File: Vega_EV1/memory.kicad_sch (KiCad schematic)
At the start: 15 parts, among them J10 1.5MB RAM Expansion, J14 Flash WR EN, J27 EXTRAM_ENABLE, P1 60 Pin Edge Conn, U5 74AHCT273, U6 74AHCT273, U7 SST39SF040, U8 AS6C1008-55PCN, U9 AS6C4008-55PCN

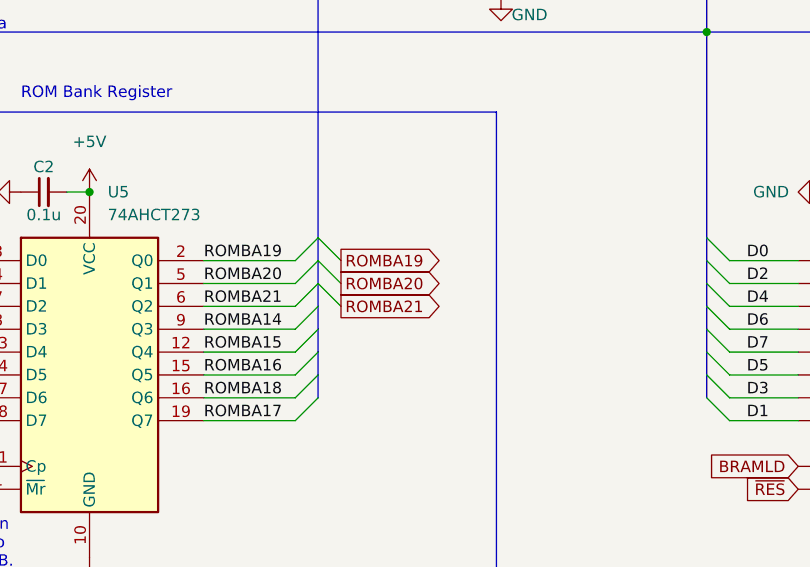
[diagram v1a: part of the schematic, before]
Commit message: More space between Edge and YM2151 Add IEC logic back in IDC headers for NES and IEC
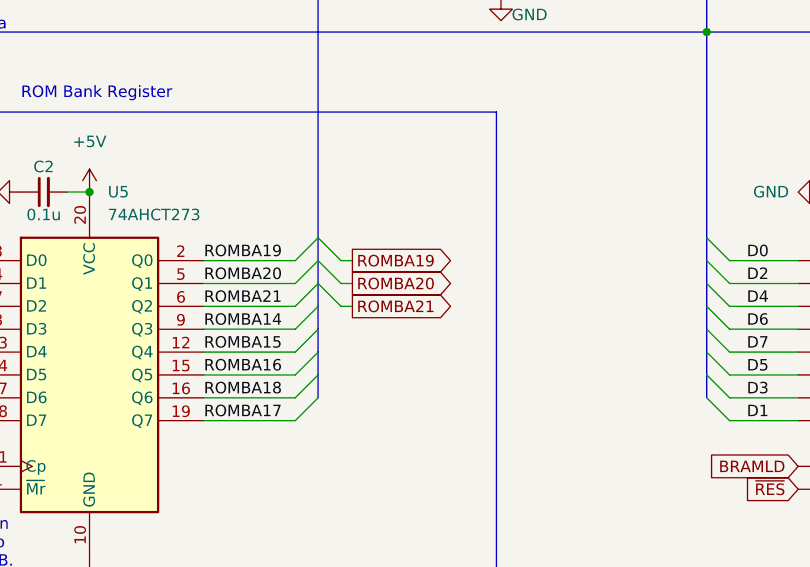
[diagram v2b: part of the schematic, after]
